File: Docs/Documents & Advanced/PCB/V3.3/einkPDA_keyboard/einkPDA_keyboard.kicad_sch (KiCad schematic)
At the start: 140 parts, among them J1 USB_C_Receptacle_USB2.0_16P, J2 Conn_01x12_Pin, J3 Conn_01x26_Pin, J4 Micro_SD_Card, J5 Conn_01x12_Pin, Q1 MMBT3904, SW36 YTS-C017-2B, SW4 SW_DIP_x02, SW41 YTS-C017-2B, U1 ESP32-S3-WROOM-1-N16R2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

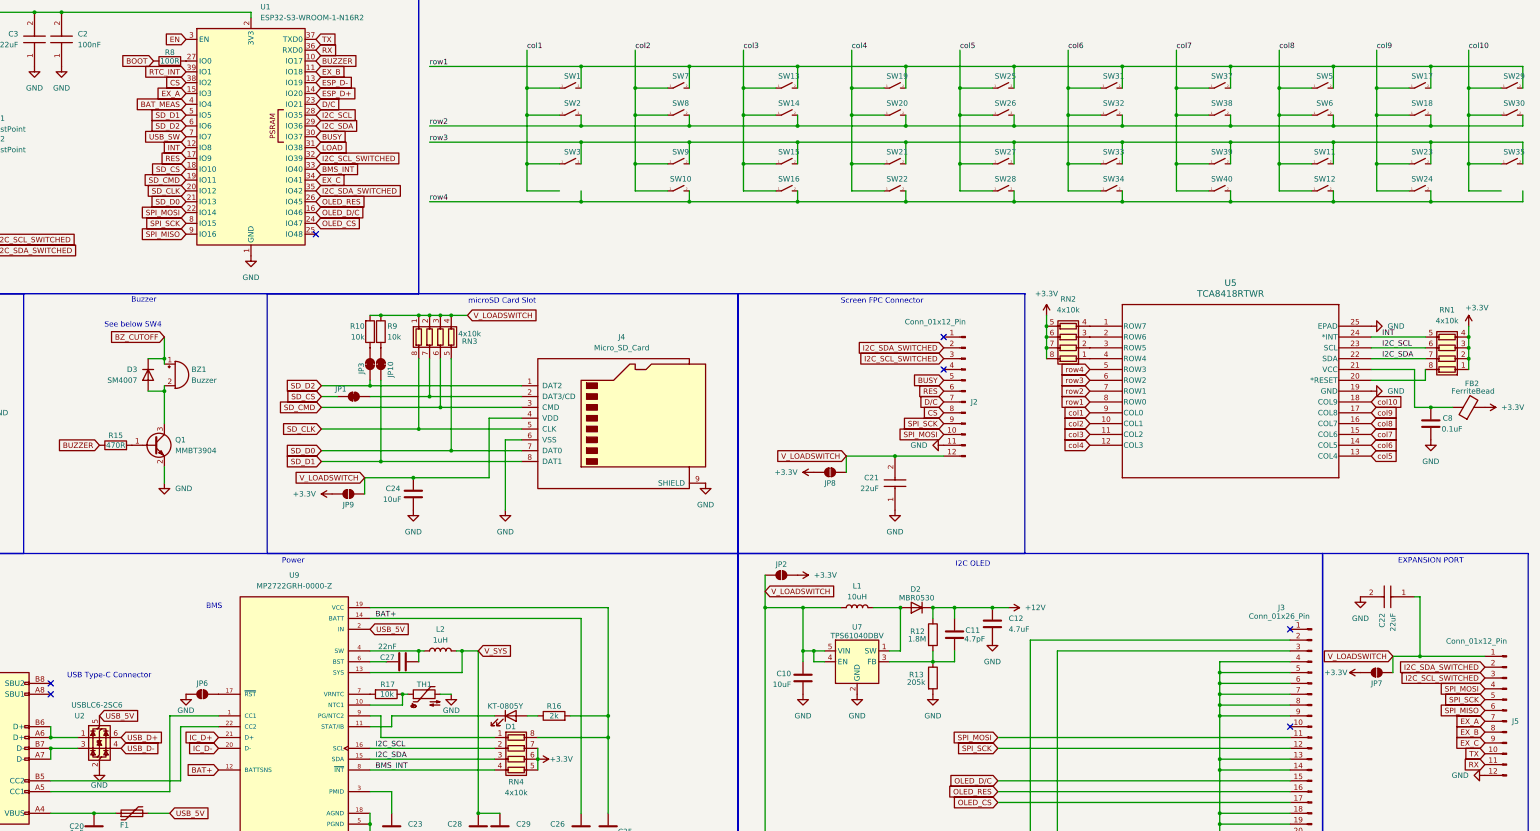
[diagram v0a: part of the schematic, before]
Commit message: Better color coding on netflags
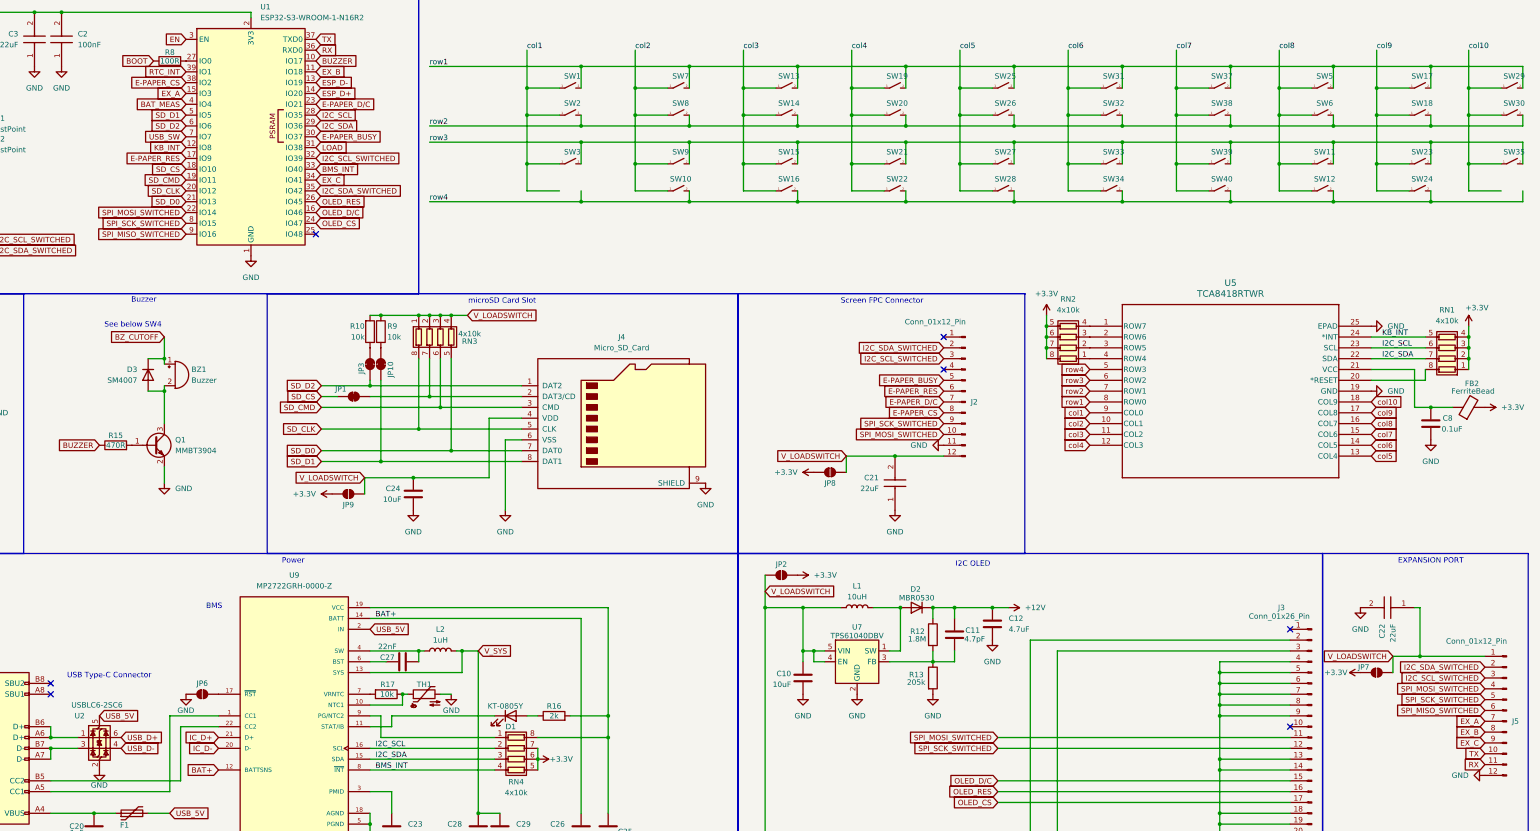
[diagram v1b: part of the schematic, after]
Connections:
- net BUSY renamed E-PAPER_BUSY
- net CS renamed E-PAPER_CS
- net D/C renamed E-PAPER_D/C
- net INT renamed KB_INT
- net RES renamed E-PAPER_RES
- net SPI_MISO renamed SPI_MISO_SWITCHED
- net SPI_MOSI renamed SPI_MOSI_SWITCHED
- net SPI_SCK renamed SPI_SCK_SWITCHED
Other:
- moved on the sheet: C22

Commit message: Update PCB with new changes
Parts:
- removed JP10, JP3: SolderJumper_2_Bridged, Jumper:SolderJumper-2_P1.3mm_Bridged_RoundedPad1.0x1.5mm, symbol Jumper:SolderJumper_2_Bridged
- removed R10, R21, R22, R9: 10k, Resistor_SMD:R_0805_2012Metric, symbol Device:R
- added RN5: 4x10k, Resistor_SMD:R_Array_Concave_4x0603, symbol Device:R_Pack04
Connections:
- net GND: now also C22.1; no longer C22.2
- net I2C_SCL_SWITCHED: now also U1.25 (IO48), RN5.7 (R2.2); no longer U1.32 (IO39)
- net I2C_SDA_SWITCHED: now also RN5.8 (R1.2)
- net SD_D1: now also RN5.5 (R4.2)
- net SD_D2: now also RN5.6 (R3.2)
- net V_LOADSWITCH: now also C22.2, RN5.1 (R1.1), RN5.2 (R2.1), RN5.3 (R3.1), RN5.4 (R4.1); no longer C22.1
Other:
- moved on the sheet: BZ1, D3, Q1, R15
